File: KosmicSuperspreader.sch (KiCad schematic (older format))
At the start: 27 parts

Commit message: Power...
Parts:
- added C? (x2): 100n, symbol Device:C_Small
- added J?: SYNTH POWER, symbol Connector_Generic:Conn_02x05_Odd_Even
- added U? (x2): TL072, symbol Amplifier_Operational:TL072
- C? (x2): value C_Small -> 100n
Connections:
- net +12V: now also C?.1, J?.10 (Pin_10), J?.9 (Pin_9), U?.8 (V+)
- net -12V: now also C?.1, J?.1 (Pin_1), J?.2 (Pin_2), U?.4 (V-)
- net GND: now also C?.2, C?.2, J?.3 (Pin_3), J?.4 (Pin_4), J?.5 (Pin_5), J?.6 (Pin_6), J?.7 (Pin_7), J?.8 (Pin_8), U?.5 (+)
- new net: U?.6 (-), U?.7
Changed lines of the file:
@@
 P 5100 5050
 F 0 "C?" V 5329 5050 50  0000 C CNN
-F 1 "C_Small" V 5238 5050 50  0000 C CNN
+F 1 "100n" V 5238 5050 50  0000 C CNN
 F 2 "" H 5100 5050 50  0001 C CNN
 F 3 "~" H 5100 5050 50  0001 C CNN
@@
 P 5100 5650
 F 0 "C?" V 5329 5650 50  0000 C CNN
-F 1 "C_Small" V 5238 5650 50  0000 C CNN
+F 1 "100n" V 5238 5650 50  0000 C CNN
 F 2 "" H 5100 5650 50  0001 C CNN
 F 3 "~" H 5100 5650 50  0001 C CNN
@@
 	5300 5300 5450 5300
 Connection ~ 5450 5300
+$Comp
+L Amplifier_Operational:TL072 U?
+U 2 1 60B4F880
+P 8150 5400
+F 0 "U?" H 8150 5767 50  0000 C CNN
+F 1 "TL072" H 8150 5676 50  0000 C CNN
+F 2 "" H 8150 5400 50  0001 C CNN
+F 3 "http://www.ti.com/lit/ds/symlink/tl071.pdf" H 8150 5400 50  0001 C CNN
+	2    8150 5400
+	1    0    0    -1
+$EndComp
+Wire Wire Line
+	8450 5400 8450 5650
+Wire Wire Line
+	8450 5650 7850 5650
+Wire Wire Line
+	7850 5650 7850 5500
+$Comp
+L power:GND #PWR?
+U 1 1 60B5124B
+P 7850 5300
+F 0 "#PWR?" H 7850 5050 50  0001 C CNN
+F 1 "GND" V 7855 5172 50  0000 R CNN
+F 2 "" H 7850 5300 50  0001 C CNN
+F 3 "" H 7850 5300 50  0001 C CNN
+	1    7850 5300
+	0    1    1    0
+$EndComp
+$Comp
+L power:+12V #PWR?
+U 1 1 60B520AE
+P 4300 5050
+F 0 "#PWR?" H 4300 4900 50  0001 C CNN
+F 1 "+12V" H 4315 5223 50  0000 C CNN
+F 2 "" H 4300 5050 50  0001 C CNN
+F 3 "" H 4300 5050 50  0001 C CNN
+	1    4300 5050
+	1    0    0    -1
+$EndComp
+$Comp
+L power:-12V #PWR?
+U 1 1 60B520B8
+P 4300 5650
+F 0 "#PWR?" H 4300 5750 50  0001 C CNN
+F 1 "-12V" H 4315 5823 50  0000 C CNN
+F 2 "" H 4300 5650 50  0001 C CNN
+F 3 "" H 4300 5650 50  0001 C CNN
+	1    4300 5650
+	-1   0    0    1
+$EndComp
+$Comp
+L Device:C_Small C?
+U 1 1 60B520C2
+P 4400 5050
+F 0 "C?" V 4629 5050 50  0000 C CNN
+F 1 "100n" V 4538 5050 50  0000 C CNN
+F 2 "" H 4400 5050 50  0001 C CNN
+F 3 "~" H 4400 5050 50  0001 C CNN
+	1    4400 5050
+	0    -1   -1   0
+$EndComp
+$Comp
+L Device:C_Small C?
+U 1 1 60B520CD
+P 4400 5650
+F 0 "C?" V 4629 5650 50  0000 C CNN
+F 1 "100n" V 4538 5650 50  0000 C CNN
+F 2 "" H 4400 5650 50  0001 C CNN
+F 3 "~" H 4400 5650 50  0001 C CNN
+	1    4400 5650
+	0    -1   -1   0
+$EndComp
+$Comp
+L power:GND #PWR?
+U 1 1 60B520D8
+P 4750 5300
+F 0 "#PWR?" H 4750 5050 50  0001 C CNN
+F 1 "GND" H 4755 5127 50  0000 C CNN
+F 2 "" H 4750 5300 50  0001 C CNN
+F 3 "" H 4750 5300 50  0001 C CNN
+	1    4750 5300
+	1    0    0    -1
+$EndComp
+Wire Wire Line
+	4500 5050 4750 5050
+Wire Wire Line
+	4750 5050 4750 5300
+Wire Wire Line
+	4500 5650 4600 5650
+Wire Wire Line
+	4600 5650 4600 5300
+Wire Wire Line
+	4600 5300 4750 5300
+Connection ~ 4750 5300
+$Comp
+L Amplifier_Operational:TL072 U?
+U 3 1 60B54907
+P 4400 5350
+F 0 "U?" H 4358 5396 50  0000 L CNN
+F 1 "TL072" H 4358 5305 50  0000 L CNN
+F 2 "" H 4400 5350 50  0001 C CNN
+F 3 "http://www.ti.com/lit/ds/symlink/tl071.pdf" H 4400 5350 50  0001 C CNN
+	3    4400 5350
+	1    0    0    -1
+$EndComp
+Connection ~ 4300 5650
+Connection ~ 4300 5050
+$Comp
+L Connector_Generic:Conn_02x05_Odd_Even J?
+U 1 1 60B55BA7
+P 2450 5350
+F 0 "J?" H 2500 5767 50  0000 C CNN
+F 1 "SYNTH POWER" H 2500 5676 50  0000 C CNN
+F 2 "" H 2450 5350 50  0001 C CNN
+F 3 "~" H 2450 5350 50  0001 C CNN
+	1    2450 5350
+	1    0    0    -1
+$EndComp
+$Comp
+L power:+12V #PWR?
+U 1 1 60B56459
+P 2500 5750
+F 0 "#PWR?" H 2500 5600 50  0001 C CNN
+F 1 "+12V" H 2515 5923 50  0000 C CNN
+F 2 "" H 2500 5750 50  0001 C CNN
+F 3 "" H 2500 5750 50  0001 C CNN
+	1    2500 5750
+	-1   0    0    1
+$EndComp
+$Comp
+L power:-12V #PWR?
+U 1 1 60B57093
+P 2500 4850
+F 0 "#PWR?" H 2500 4950 50  0001 C CNN
+F 1 "-12V" H 2515 5023 50  0000 C CNN
+F 2 "" H 2500 4850 50  0001 C CNN
+F 3 "" H 2500 4850 50  0001 C CNN
+	1    2500 4850
+	1    0    0    -1
+$EndComp
+Wire Wire Line
+	2750 5150 2750 4850
+Wire Wire Line
+	2750 4850 2500 4850
+Wire Wire Line
+	2500 4850 2250 4850
+Wire Wire Line
+	2250 4850 2250 5150
+Connection ~ 2500 4850
+Wire Wire Line
+	2750 5550 2750 5750
+Wire Wire Line
+	2750 5750 2500 5750
+Wire Wire Line
+	2250 5550 2250 5750
+Wire Wire Line
+	2250 5750 2500 5750
+Connection ~ 2500 5750
+$Comp
+L power:GND #PWR?
+U 1 1 60B5DFE3
+P 2850 5350
+F 0 "#PWR?" H 2850 5100 50  0001 C CNN
+F 1 "GND" V 2855 5222 50  0000 R CNN
+F 2 "" H 2850 5350 50  0001 C CNN
+F 3 "" H 2850 5350 50  0001 C CNN
+	1    2850 5350
+	0    -1   -1   0
+$EndComp
+Wire Wire Line
+	2750 5250 2850 5250
+Wire Wire Line
+	2850 5250 2850 5350
+Wire Wire Line
+	2750 5350 2850 5350
+Connection ~ 2850 5350
+Wire Wire Line
+	2750 5450 2850 5450
+Wire Wire Line
+	2850 5450 2850 5350
+$Comp
+L power:GND #PWR?
+U 1 1 60B63CE1
+P 2100 5350
+F 0 "#PWR?" H 2100 5100 50  0001 C CNN
+F 1 "GND" V 2105 5222 50  0000 R CNN
+F 2 "" H 2100 5350 50  0001 C CNN
+F 3 "" H 2100 5350 50  0001 C CNN
+	1    2100 5350
+	0    1    1    0
+$EndComp
+Wire Wire Line
+	2250 5250 2100 5250
+Wire Wire Line
+	2100 5250 2100 5350
+Wire Wire Line
+	2250 5350 2100 5350
+Connection ~ 2100 5350
+Wire Wire Line
+	2250 5450 2100 5450
+Wire Wire Line
+	2100 5450 2100 5350
 $EndSCHEMATC

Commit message: More decoupling
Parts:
- added C? (x2): 10u, symbol Device:CP_Small
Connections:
- net +12V: now also C?.1
- net -12V: now also C?.2
- net GND: now also C?.1, C?.2
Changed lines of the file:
@@
 Wire Wire Line
 	2100 5450 2100 5350
+$Comp
+L Device:CP_Small C?
+U 1 1 60B6A76C
+P 3500 5200
+F 0 "C?" H 3588 5246 50  0000 L CNN
+F 1 "10u" H 3588 5155 50  0000 L CNN
+F 2 "" H 3500 5200 50  0001 C CNN
+F 3 "~" H 3500 5200 50  0001 C CNN
+	1    3500 5200
+	1    0    0    -1
+$EndComp
+$Comp
+L Device:CP_Small C?
+U 1 1 60B6B00C
+P 3500 5400
+F 0 "C?" H 3588 5446 50  0000 L CNN
+F 1 "10u" H 3588 5355 50  0000 L CNN
+F 2 "" H 3500 5400 50  0001 C CNN
+F 3 "~" H 3500 5400 50  0001 C CNN
+	1    3500 5400
+	1    0    0    -1
+$EndComp
+$Comp
+L power:+12V #PWR?
+U 1 1 60B6B2BA
+P 3500 5100
+F 0 "#PWR?" H 3500 4950 50  0001 C CNN
+F 1 "+12V" H 3515 5273 50  0000 C CNN
+F 2 "" H 3500 5100 50  0001 C CNN
+F 3 "" H 3500 5100 50  0001 C CNN
+	1    3500 5100
+	1    0    0    -1
+$EndComp
+$Comp
+L power:-12V #PWR?
+U 1 1 60B6BA9A
+P 3500 5500
+F 0 "#PWR?" H 3500 5600 50  0001 C CNN
+F 1 "-12V" H 3515 5673 50  0000 C CNN
+F 2 "" H 3500 5500 50  0001 C CNN
+F 3 "" H 3500 5500 50  0001 C CNN
+	1    3500 5500
+	-1   0    0    1
+$EndComp
+$Comp
+L power:GND #PWR?
+U 1 1 60B6BEDA
+P 3500 5300
+F 0 "#PWR?" H 3500 5050 50  0001 C CNN
+F 1 "GND" V 3505 5172 50  0000 R CNN
+F 2 "" H 3500 5300 50  0001 C CNN
+F 3 "" H 3500 5300 50  0001 C CNN
+	1    3500 5300
+	0    1    1    0
+$EndComp
+Connection ~ 3500 5300
 $EndSCHEMATC

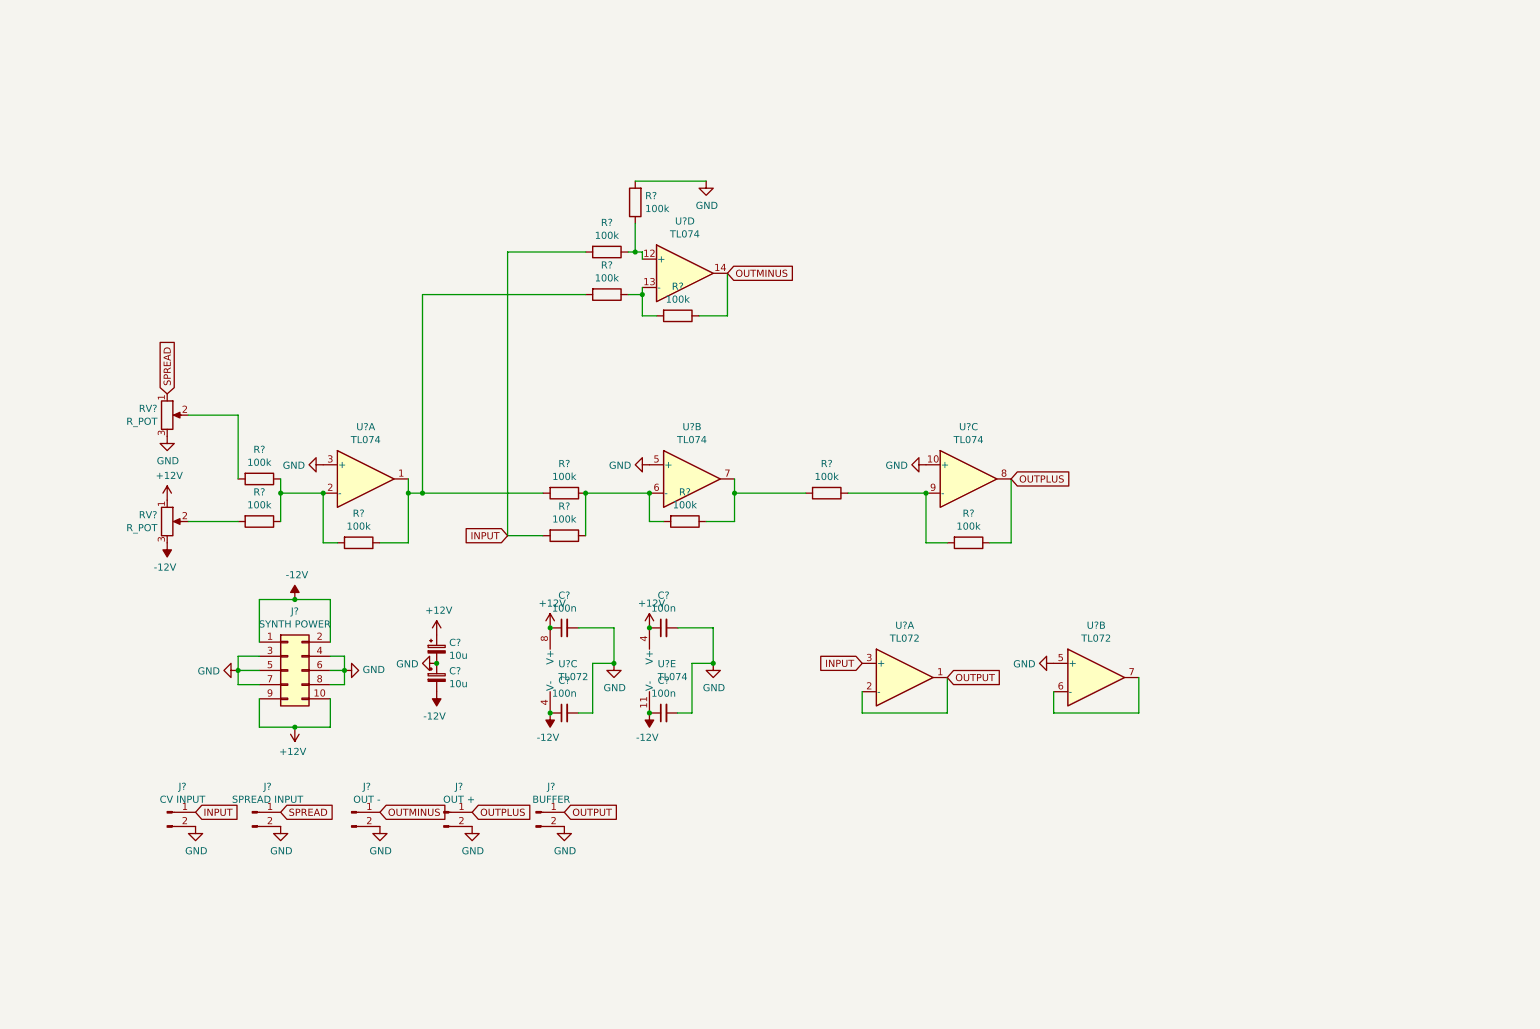
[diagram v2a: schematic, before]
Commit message: Clean up, add explanatory text, not tested
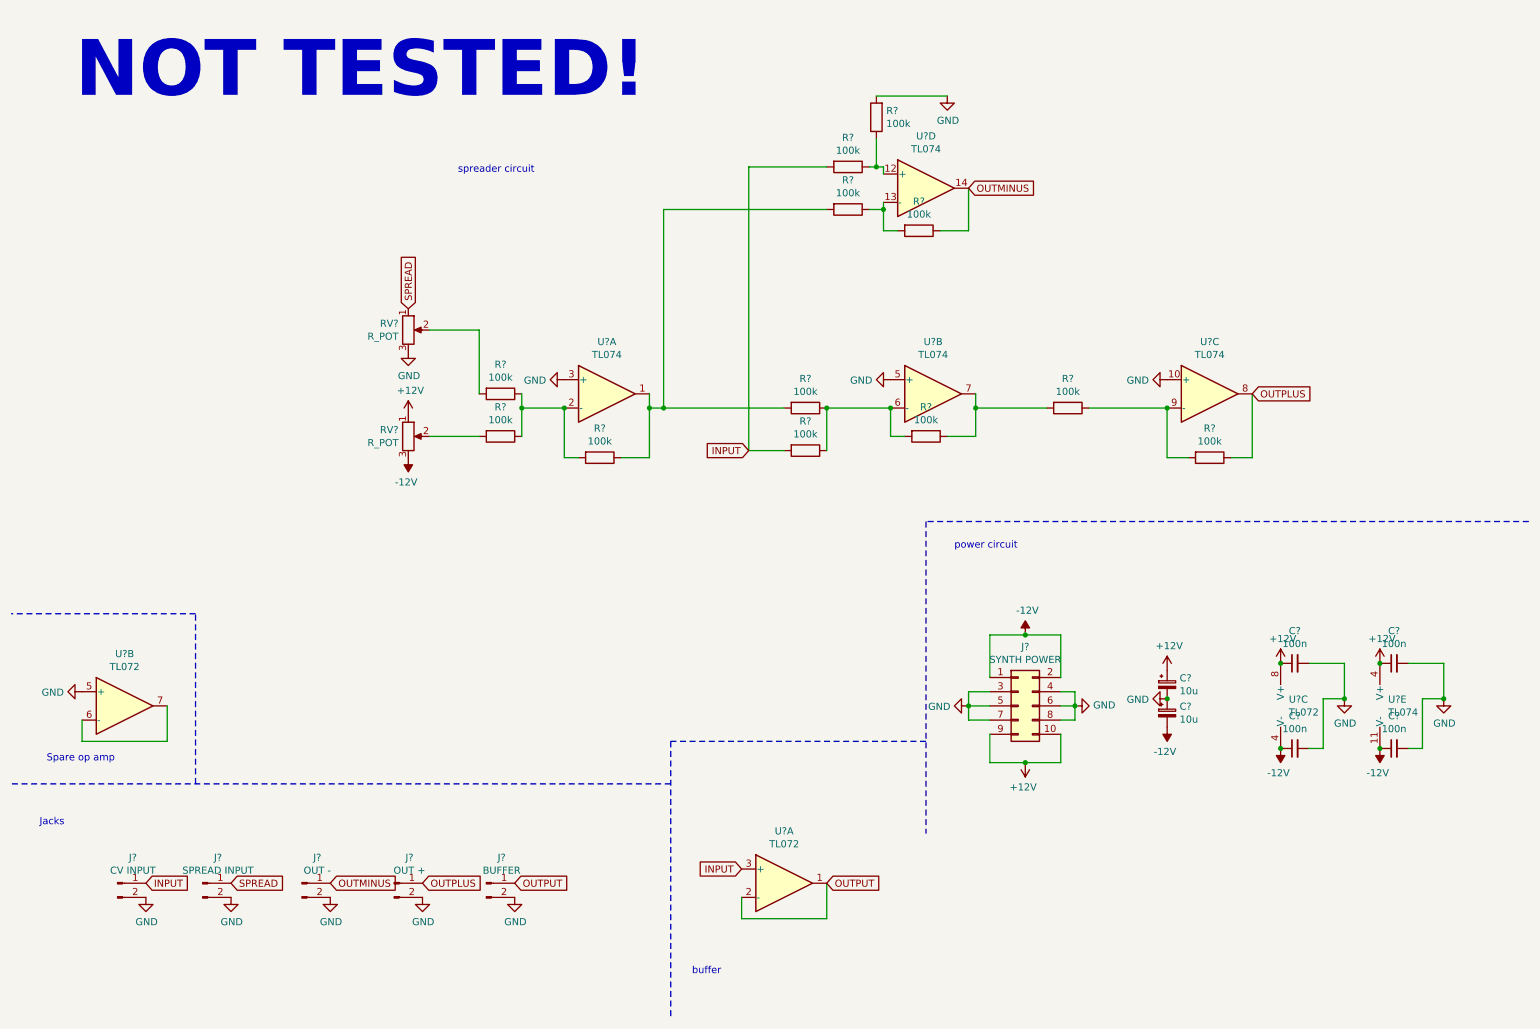
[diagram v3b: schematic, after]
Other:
- note added: "Jacks\n"
- note added: "NOT TESTED!"
- note added: "Spare op amp"
- note added: "buffer"
- note added: "power circuit"
- note added: "spreader circuit"
- moved on the sheet: C?, J?, R?, RV?, U?A, U?B, U?C, U?D, U?E
